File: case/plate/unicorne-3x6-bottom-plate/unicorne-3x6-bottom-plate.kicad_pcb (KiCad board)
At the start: 2 copper layers, 114.8 x 91.4 mm, 6 parts, among them J3 Tenting Puck

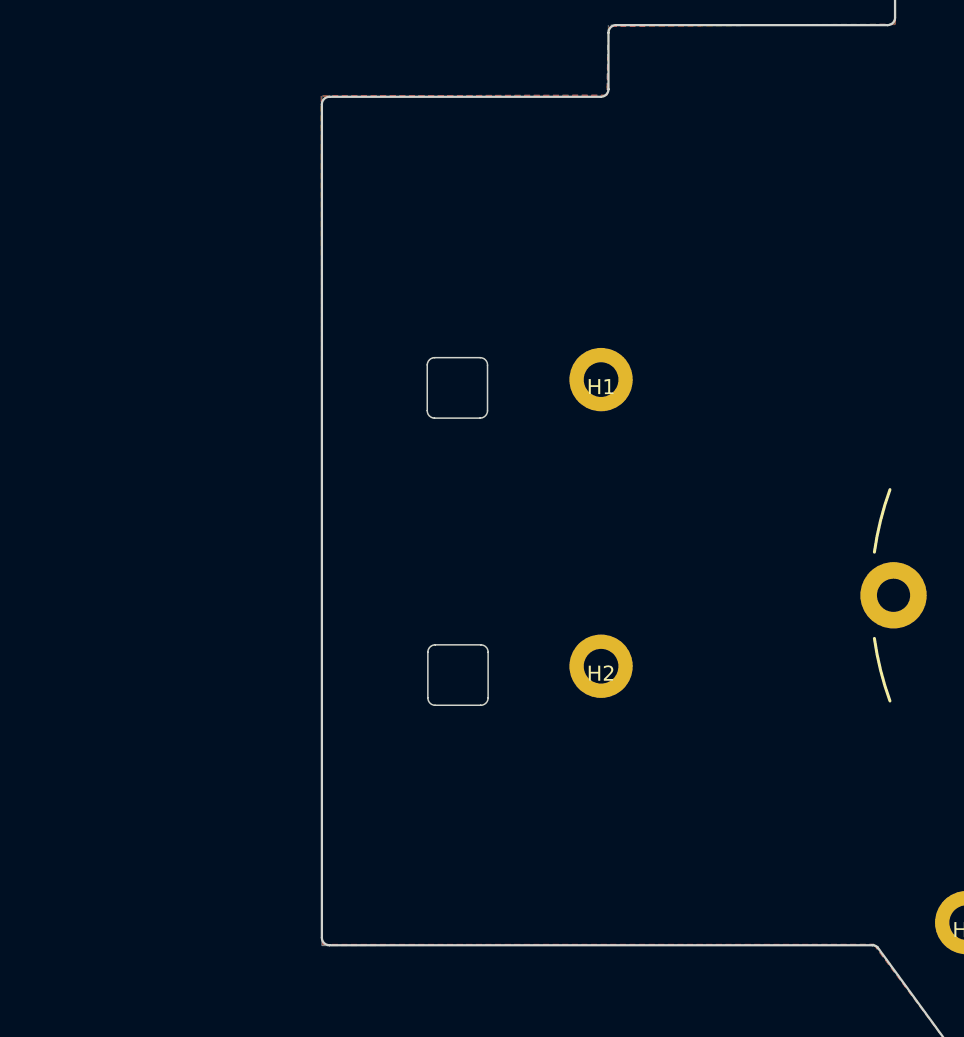
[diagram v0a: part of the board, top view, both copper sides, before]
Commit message: added plates
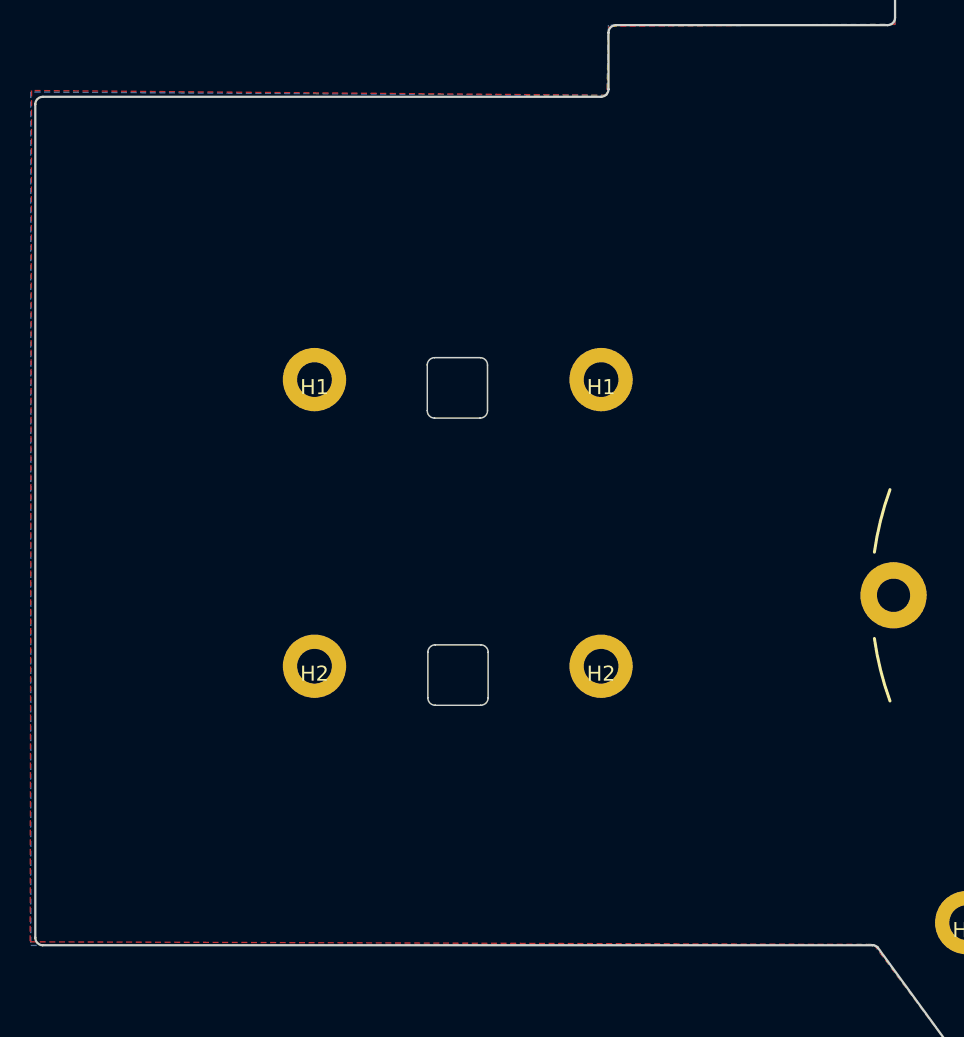
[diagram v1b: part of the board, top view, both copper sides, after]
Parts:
- added H1: MountingHole, KBD_PARTS:M2_Hole_TH, F.Cu at (79.4, 86.8)
- added H2: MountingHole, KBD_PARTS:M2_Hole_TH, F.Cu at (79.4, 105.8)
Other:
- board size 114.8 x 91.4 mm -> 133.8 x 91.4 mm
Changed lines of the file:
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@@
+  )
+  (footprint "KBD_PARTS:M2_Hole_TH" locked (layer "F.Cu")
+    (at 79.39 105.846905)
+    (property "Sheetfile" "unicorne-3x5-bottom-plate.kicad_sch")
+    (property "Sheetname" "")
+    (property "ki_description" "Mounting Hole without connection")
+    (property "ki_keywords" "mounting hole")
+    (attr through_hole)
+    (fp_text reference "H2" (at 0 0.5) (layer "F.SilkS")
+        (effects (font (size 1 1) (thickness 0.15)))
+    )
+    (fp_text value "MountingHole" (at 0 -0.5) (layer "F.Fab")
+        (effects (font (size 1 1) (thickness 0.15)))
+    )
+    (pad "" thru_hole circle locked (at 0 0.003095) (size 4.2 4.2) (drill 2.3) (layers "*.Cu" "*.Mask"))
+  )
+  (footprint "KBD_PARTS:M2_Hole_TH" locked (layer "F.Cu")
+    (at 79.39 86.846905)
+    (property "Sheetfile" "unicorne-3x5-bottom-plate.kicad_sch")
+    (property "Sheetname" "")
+    (property "ki_description" "Mounting Hole without connection")
+    (property "ki_keywords" "mounting hole")
+    (attr through_hole)
+    (fp_text reference "H1" (at 0 0.5) (layer "F.SilkS")
+        (effects (font (size 1 1) (thickness 0.15)))
+    )
+    (fp_text value "MountingHole" (at 0 -0.5) (layer "F.Fab")
+        (effects (font (size 1 1) (thickness 0.15)))
+    )
+    (pad "" thru_hole circle locked (at 0 0) (size 4.2 4.2) (drill 2.3) (layers "*.Cu" "*.Mask"))
   )
   (footprint "KBD_PARTS:M2_Hole_TH" locked (layer "F.Cu")
@@
   (gr_circle (center 155.39 83.096905) (end 156.54 83.096905)
     (stroke (width 0.15) (type default)) (fill none) (layer "Eco1.User"))
+  (gr_circle (center 79.39 105.846905) (end 80.54 105.846905)
+    (stroke (width 0.15) (type default)) (fill none) (layer "Eco1.User"))
   (gr_circle (center 98.39 105.846905) (end 99.54 105.846905)
     (stroke (width 0.15) (type default)) (fill none) (layer "Eco1.User"))
@@
   (gr_circle (center 122.64 122.846905) (end 123.79 122.846905)
     (stroke (width 0.15) (type default)) (fill none) (layer "Eco1.User"))
+  (gr_circle (center 79.39 86.846905) (end 80.54 86.846905)
+    (stroke (width 0.15) (type default)) (fill none) (layer "Eco1.User"))
   (gr_line (start 155.39 83.096905) (end 155.38 83.096905)
     (stroke (width 2.5) (type solid)) (layer "Eco2.User"))
   (gr_line (start 122.64 122.846905) (end 122.63 122.846905)
     (stroke (width 2.5) (type solid)) (layer "Eco2.User"))
+  (gr_line (start 79.39 86.846905) (end 79.38 86.846905)
+    (stroke (width 2.5) (type solid)) (layer "Eco2.User"))
   (gr_line (start 98.39 86.846905) (end 98.38 86.846905)
+    (stroke (width 2.5) (type solid)) (layer "Eco2.User"))
+  (gr_line (start 79.39 105.846905) (end 79.38 105.846905)
     (stroke (width 2.5) (type solid)) (layer "Eco2.User"))
   (gr_line (start 169.14 130.596905) (end 169.13 130.596905)
@@
   (gr_arc (start 166.383433 83.062084) (mid 166.725167 83.209566) (end 166.863433 83.555132)
     (stroke (width 0.1) (type default)) (layer "Edge.Cuts"))
-  (gr_line (start 98.38 68.096905) (end 80.38 68.096905)
+  (gr_line (start 98.38 68.096905) (end 61.38 68.096905)
     (stroke (width 0.15) (type solid)) (layer "Edge.Cuts"))
   (gr_line (start 117.38 63.346905) (end 99.38 63.346905)
@@
   (gr_line (start 128.403433 116.432084) (end 125.380204 116.432084)
     (stroke (width 0.1) (type default)) (layer "Edge.Cuts"))
-  (gr_arc (start 80.38 124.346905) (mid 80.026447 124.200458) (end 79.88 123.846905)
+  (gr_arc (start 61.38 124.346905) (mid 61.026445 124.200459) (end 60.88 123.846905)
     (stroke (width 0.15) (type solid)) (layer "Edge.Cuts"))
   (gr_arc (start 164.300556 143.867249) (mid 164.630952 143.916054) (end 164.955 143.996905)
@@
   (gr_arc (start 90.900792 107.950338) (mid 90.755347 108.293993) (end 90.410385 108.436309)
     (stroke (width 0.1) (type default)) (layer "Edge.Cuts"))
-  (gr_line (start 116.38 124.346905) (end 80.38 124.346905)
+  (gr_line (start 116.38 124.346905) (end 61.38 124.346905)
     (stroke (width 0.15) (type solid)) (layer "Edge.Cuts"))
   (gr_line (start 127.63 139.096905) (end 164.300556 143.867249)
@@
   (gr_arc (start 173.38 65.846905) (mid 173.733553 65.993352) (end 173.88 66.346905)
     (stroke (width 0.15) (type solid)) (layer "Edge.Cuts"))
-  (gr_line (start 79.88 68.596905) (end 79.88 123.846905)
+  (gr_line (start 60.88 68.596905) (end 60.88 123.846905)
     (stroke (width 0.15) (type solid)) (layer "Edge.Cuts"))
   (gr_line (start 90.383433 85.393472) (end 87.360204 85.393472)
@@
   (gr_line (start 164.955 143.996905) (end 179.28 152.271905)
     (stroke (width 0.15) (type solid)) (layer "Edge.Cuts"))
-  (gr_arc (start 79.88 68.596905) (mid 80.026447 68.243352) (end 80.38 68.096905)
+  (gr_arc (start 60.88 68.596905) (mid 61.026445 68.243348) (end 61.38 68.096905)
     (stroke (width 0.15) (type solid)) (layer "Edge.Cuts"))
   (gr_line (start 166.910792 124.650338) (end 166.910792 121.625132)
@@
   (gr_line (start 173.88 66.346905) (end 173.88 67.596905)
     (stroke (width 0.15) (type solid)) (layer "Edge.Cuts"))
+  (gr_line (start 79.38 84.396905) (end 79.38 89.296968)
+    (stroke (width 0.1) (type solid)) (layer "F.Fab"))
   (gr_line (start 169.13 128.146905) (end 169.13 133.046968)
     (stroke (width 0.1) (type solid)) (layer "F.Fab"))
+  (gr_line (start 76.93 86.846905) (end 81.83 86.846905)
+    (stroke (width 0.1) (type solid)) (layer "F.Fab"))
   (gr_line (start 98.38 103.396905) (end 98.38 108.296968)
     (stroke (width 0.1) (type solid)) (layer "F.Fab"))
@@
     (stroke (width 0.1) (type solid)) (layer "F.Fab"))
   (gr_line (start 120.18 122.846905) (end 125.08 122.846905)
+    (stroke (width 0.1) (type solid)) (layer "F.Fab"))
+  (gr_line (start 76.93 105.846905) (end 81.83 105.846905)
+    (stroke (width 0.1) (type solid)) (layer "F.Fab"))
+  (gr_line (start 79.38 103.396905) (end 79.38 108.296968)
     (stroke (width 0.1) (type solid)) (layer "F.Fab"))
   (gr_line (start 95.93 86.846905) (end 100.83 86.846905)
@@
         (xy 98.91 63.43)
         (xy 98.78 67.996905)
-        (xy 79.84 68.05)
-        (xy 79.91 124.3)
+        (xy 60.63 67.68)
+        (xy 60.54 124.12)
         (xy 116.48 124.296905)
         (xy 127.48 139.096905)
@@
         (xy 98.88 63.35)
         (xy 98.78 67.996905)
-        (xy 79.87 68.04)
-        (xy 79.88 124.37)
+        (xy 60.58 67.78)
+        (xy 60.58 124.36)
         (xy 116.48 124.296905)
         (xy 127.48 139.096905)
